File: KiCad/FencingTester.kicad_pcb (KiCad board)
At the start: 2 copper layers, 114.5 x 60.5 mm, 63 parts, among them IC1 ATMEGA328P-P, P1 SERIAL, P2 CONN_01X03, P3 CONN_01X03, P4 USB_OTG, SW1 SP3T, SW2 SP3T, SW3 SPST, U1 TLC59116, U2 MCP73831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

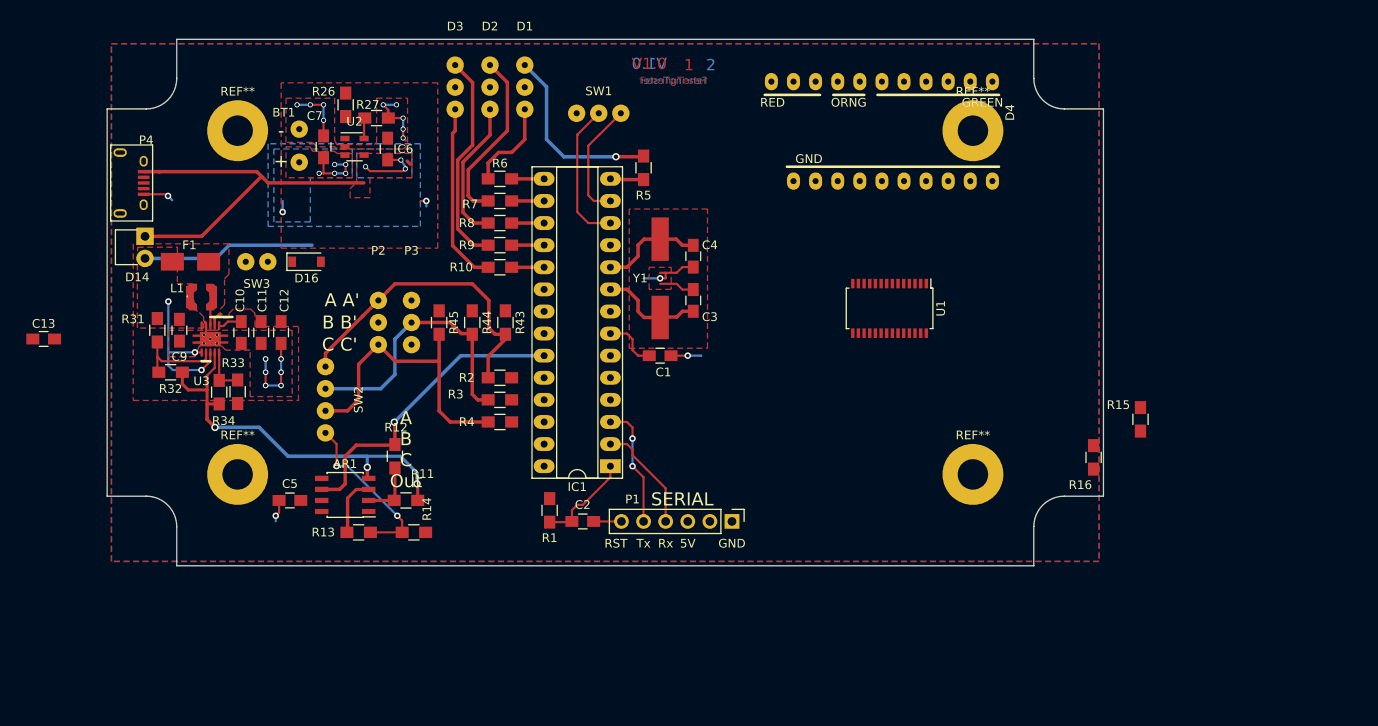
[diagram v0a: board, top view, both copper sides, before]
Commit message: Updating modules libraries
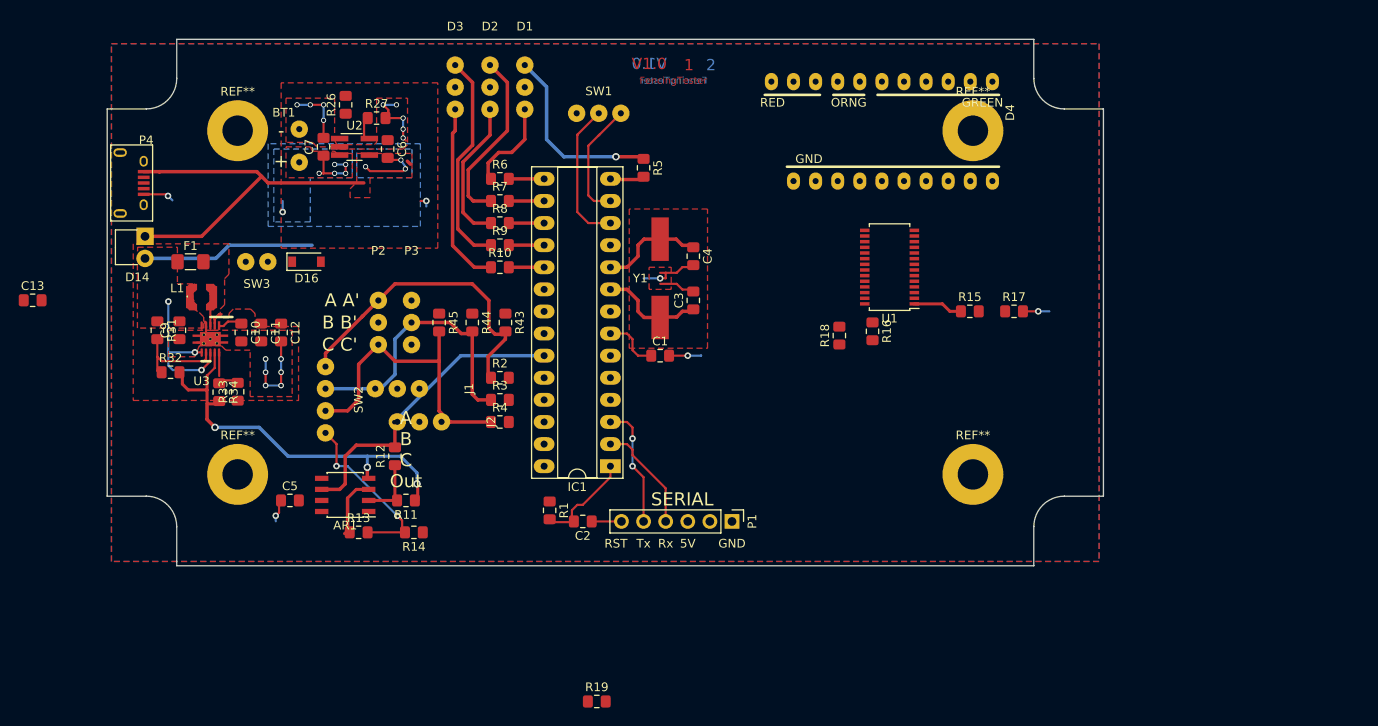
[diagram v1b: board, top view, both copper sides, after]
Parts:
- added J1: Conn_01x03_Female, custom-fencingTester:3PadsWires, F.Cu at (133.3, 57.1)
- added J2: Conn_01x03_Female, custom-fencingTester:3PadsWires, F.Cu at (135.9, 61.0)
- added R17: 330, Resistor_SMD:R_0805_2012Metric_Pad1.15x1.40mm_HandSolder, F.Cu at (204.2, 48.3)
- added R18: 10k, Resistor_SMD:R_0805_2012Metric_Pad1.15x1.40mm_HandSolder, F.Cu at (184.2, 51.0)
- added R19: 10k, Resistor_SMD:R_0805_2012Metric_Pad1.15x1.40mm_HandSolder, F.Cu at (156.3, 93.1)
- AR1: footprint Housings_SOIC:SOIC-8_3.9x4.9mm_Pitch1.27mm -> Package_SO:SOIC-8_3.9x4.9mm_P1.27mm
- C1, C10, C11, C12, C13, C2, C3, C4, C5, C6, C7, C9: footprint Capacitors_SMD:C_0805_HandSoldering -> Capacitor_SMD:C_0805_2012Metric_Pad1.15x1.40mm_HandSolder
- F1: footprint Fuse_Holders_and_Fuses:Fuse_SMD1206_HandSoldering -> Fuse:Fuse_1206_3216Metric_Pad1.42x1.75mm_HandSolder
- IC1: footprint Housings_DIP:DIP-28_W7.62mm_Socket_LongPads -> Package_DIP:DIP-28_W7.62mm_Socket_LongPads
- P1: footprint Pin_Headers:Pin_Header_Straight_1x06_Pitch2.54mm -> Connector_PinHeader_2.54mm:PinHeader_1x06_P2.54mm_Vertical
- R1, R10, R11, R12, R13, R14, R16, R2, R26, R27, R3, R31, R32, R33, R34, R4, R43, R44, R45, R5, R6, R7, R8, R9: footprint Resistors_SMD:R_0805_HandSoldering -> Resistor_SMD:R_0805_2012Metric_Pad1.15x1.40mm_HandSolder
- R15: value R -> 330; footprint Resistors_SMD:R_0805_HandSoldering -> Resistor_SMD:R_0805_2012Metric_Pad1.15x1.40mm_HandSolder
- U1: footprint Housings_SSOP:TSSOP-28_4.4x9.7mm_Pitch0.65mm -> Package_SO:TSSOP-28_4.4x9.7mm_P0.65mm
- U2: footprint TO_SOT_Packages_SMD:SOT-23-5 -> Package_TO_SOT_SMD:TSOT-23-5_HandSoldering
- moved R16 29.2 mm to (188.0, 50.6)
- moved R15 23.2 mm to (199.1, 48.3), turned to 0 degrees
- moved U1 4.74 mm to (189.9, 43.2), turned to 180 degrees
- moved C13 4.62 mm to (91.4, 47.0)
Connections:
- IC1 pad 11: (no net) -> Net-(IC1-Pad11)
- IC1 pad 21: (no net) -> Net-(IC1-Pad21)
- IC1 pad 25: (no net) -> Net-(IC1-Pad25)
- IC1 pad 26: (no net) -> Net-(IC1-Pad26)
- P1 pad 2: (no net) -> Net-(P1-Pad2)
- P4 pad 2: (no net) -> Net-(P4-Pad2)
- P4 pad 3: (no net) -> Net-(P4-Pad3)
- P4 pad 4: (no net) -> Net-(P4-Pad4)
- R15 pad 2: GND -> Net-(R15-Pad2)
- U1 pad 22: (no net) -> Net-(U1-Pad22)
- U1 pad 23: (no net) -> Net-(U1-Pad23)
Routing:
- net Net-(R15-Pad1): track 0.00 -> 5.70 mm
- net GND: track 51.7 -> 54.7 mm, vias 20 -> 21

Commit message: PCB advancements
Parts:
- moved R15 7.24 mm to (192.2, 46.4)
- moved R17 7.24 mm to (197.2, 46.4)
- moved U1 5.91 mm to (184.2, 41.9)
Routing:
- net /CAA': track 35.9 -> 0.08 mm
- net /CCC': track 34.7 -> 0.37 mm
- net /CBB': track 32.0 -> 0.11 mm
- net /Rsense: track 35.4 -> 12.4 mm, vias 1 -> 0
- net Net-(D4-Pad30): track 0.00 -> 21.6 mm
- net Net-(D14-Pad1): track 19.8 -> 0.00 mm
- net Net-(D4-Pad29): track 0.00 -> 18.0 mm
- net Net-(D4-Pad28): track 0.00 -> 13.8 mm
- net Net-(D4-Pad27): track 0.00 -> 11.7 mm
- net Net-(D4-Pad26): track 0.00 -> 9.77 mm
- net GND: track 54.7 -> 63.5 mm, vias 21 -> 25
- net Net-(D4-Pad24): track 0.00 -> 7.74 mm
- net Net-(D4-Pad25): track 0.00 -> 7.34 mm
- net Net-(D4-Pad21): track 0.00 -> 7.22 mm
- net Net-(D4-Pad23): track 0.00 -> 6.82 mm
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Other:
- net class sensitive_tracks: trace_width 0.4 -> 0.25

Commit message: [WIP] PCB layout
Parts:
- removed P2, P3: CONN_01X03, custom-fencingTester:3PadsWires
- moved R19 99.8 mm to (234.9, 31.8)
- moved C5 54.7 mm to (168.3, 42.5), turned to 180 degrees
- moved R15 52.4 mm to (237.2, 19.7)
- moved R18 52.4 mm to (229.2, 24.4)
- moved R16 52.4 mm to (233.0, 23.9)
- moved R17 52.4 mm to (242.3, 19.7)
- moved SW1 48.0 mm to (191.0, 58.8), turned to 90 degrees
- moved AR1 45.3 mm to (161.9, 40.0)
- moved R11 44.9 mm to (168.3, 40.6)
- moved R12 44.0 mm to (167.0, 36.8)
- moved R13 43.7 mm to (161.9, 45.1)
- moved R14 42.2 mm to (166.4, 45.1)
- moved R6 40.9 mm to (183.5, 47.2), turned to 270 degrees
- moved D1 40.7 mm to (184.8, 40.0), turned to 270 degrees
- moved D2 39.8 mm to (179.7, 40.0)
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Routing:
- net /BSense: track 0.00 -> 64.9 mm, vias 0 -> 1
- net GNDA: track 47.2 -> 93.4 mm
- net Net-(D14-Pad1): track 0.00 -> 41.4 mm, vias 0 -> 1
- net /CBB': track 0.11 -> 38.0 mm, vias 0 -> 2
- net /CCC': track 0.37 -> 23.3 mm
- net /CAA': track 0.08 -> 22.7 mm
- net Net-(D4-Pad30): track 21.6 -> 0.00 mm
- net Net-(D4-Pad29): track 18.0 -> 0.00 mm
- net Net-(D3-Pad1): track 20.9 -> 4.19 mm
- net Net-(R13-Pad2): track 19.5 -> 34.8 mm, vias 2 -> 1
- net Net-(D3-Pad3): track 24.6 -> 9.80 mm
- net /Rsense: track 12.4 -> 27.2 mm
- net Net-(D4-Pad28): track 13.8 -> 0.00 mm
- net Net-(IC1-Pad6): track 0.00 -> 12.4 mm
- net Net-(D2-Pad1): track 16.5 -> 4.19 mm
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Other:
- board text removed: "A B C Out"
